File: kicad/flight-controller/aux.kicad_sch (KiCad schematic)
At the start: 5 parts, among them J11 Inter ESP UART

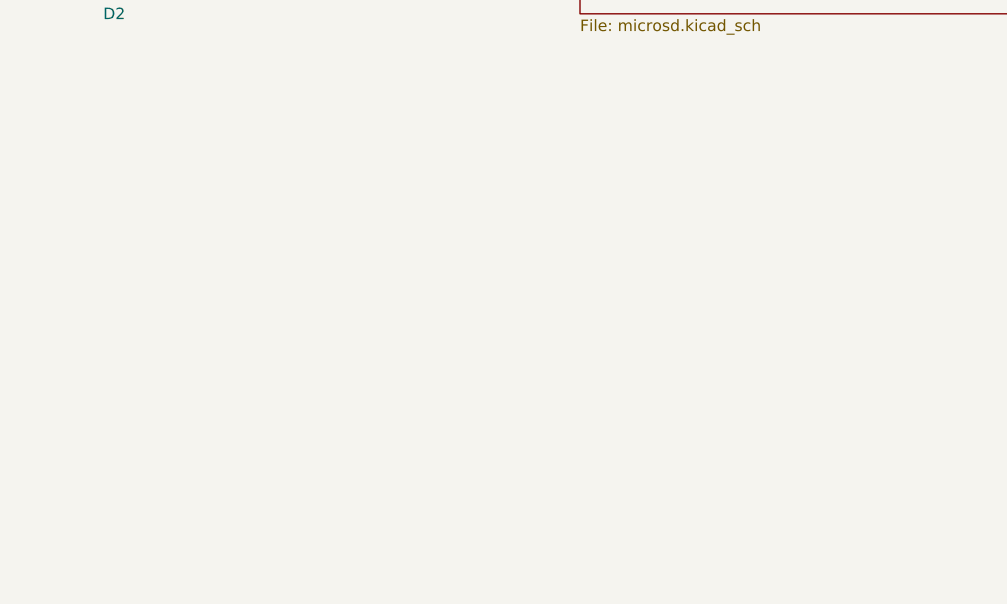
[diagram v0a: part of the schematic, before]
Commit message: removed basestation code and v3.1 of fc pcb
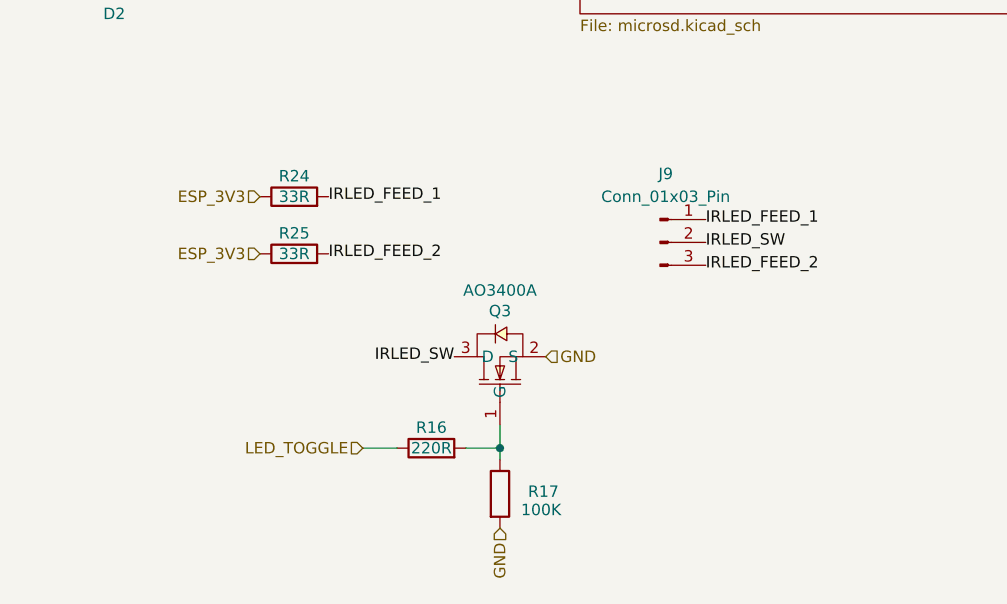
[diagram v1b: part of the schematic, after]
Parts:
- added J9: Conn_01x03_Pin, Connector_JST:JST_GH_BM03B-GHS-TBT_1x03-1MP_P1.25mm_Vertical, symbol Connector:Conn_01x03_Pin
- added Q3: AO3400A, easyeda2kicad:SOT-23-3_L2.9-W1.3-P1.90-LS2.4-BR, symbol easyeda2kicad:AO3400A
- added R16: 220R, Resistor_SMD:R_0402_1005Metric, symbol Device:R
- added R17: 100K, Resistor_SMD:R_0402_1005Metric, symbol Device:R
- added R24, R25: 33R, Resistor_SMD:R_1206_3216Metric, symbol Device:R
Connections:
- net ESP_3V3: now also R24.1, R25.1
- net GND: now also Q3.2 (S), R17.2
- new net: Q3.1 (G), R16.2, R17.1
- new net IRLED_FEED_1: J9.1 (Pin_1), R24.2
- new net IRLED_FEED_2: J9.3 (Pin_3), R25.2
- new net IRLED_SW: J9.2 (Pin_2), Q3.3 (D)
- new net LED_TOGGLE: R16.1

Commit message: Kicad FC v3.1 complete, Mission Controller and UWB boards v1 complete, firmware v2 complete!
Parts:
- J9: LCSC Part (none) -> C161691
- R24, R25: LCSC Part (none) -> C5759775
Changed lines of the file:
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@@
 		)
 	)
-	(hierarchical_label "MOSI"
+	(hierarchical_label "SD_MOSI"
 		(shape input)
 		(at 151.13 99.06 180)
@@
 		)
 	)
-	(hierarchical_label "MISO"
+	(hierarchical_label "SD_MISO"
 		(shape output)
 		(at 200.66 102.87 0)
@@
 		)
 	)
-	(hierarchical_label "SCK"
+	(hierarchical_label "SD_SCK"
 		(shape input)
 		(at 151.13 102.87 180)
@@
 		)
 		(property "Description" "IR LED current-limit resistor -- verify value against actual LED Vf/battery voltage before fab"
+			(at 119.38 135.89 0)
+			(hide yes)
+			(show_name no)
+			(do_not_autoplace no)
+			(effects
+				(font
+					(size 1.27 1.27)
+				)
+			)
+		)
+		(property "LCSC Part" "C5759775"
 			(at 119.38 135.89 0)
 			(hide yes)
@@
 			)
 		)
+		(property "LCSC Part" "C161691"
+			(at 160.02 140.97 0)
+			(hide yes)
+			(show_name no)
+			(do_not_autoplace no)
+			(effects
+				(font
+					(size 1.27 1.27)
+				)
+			)
+		)
 		(pin "1"
 		)
@@
 			(at 119.38 142.24 0)
 			(hide yes)
+			(show_name no)
+			(do_not_autoplace no)
+			(effects
+				(font
+					(size 1.27 1.27)
+				)
+			)
+		)
+		(property "LCSC Part" "C5759775"
+			(at 119.38 142.24 0)
+			(hide yes)
